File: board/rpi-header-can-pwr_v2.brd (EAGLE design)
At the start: 87 x 56.5 mm, 57 parts, among them U1 MCP2515, U2 ADS1015, U3 BME280, X1 RJ45-8L21-S, X2 RASPI_BOARD_B+#_E3

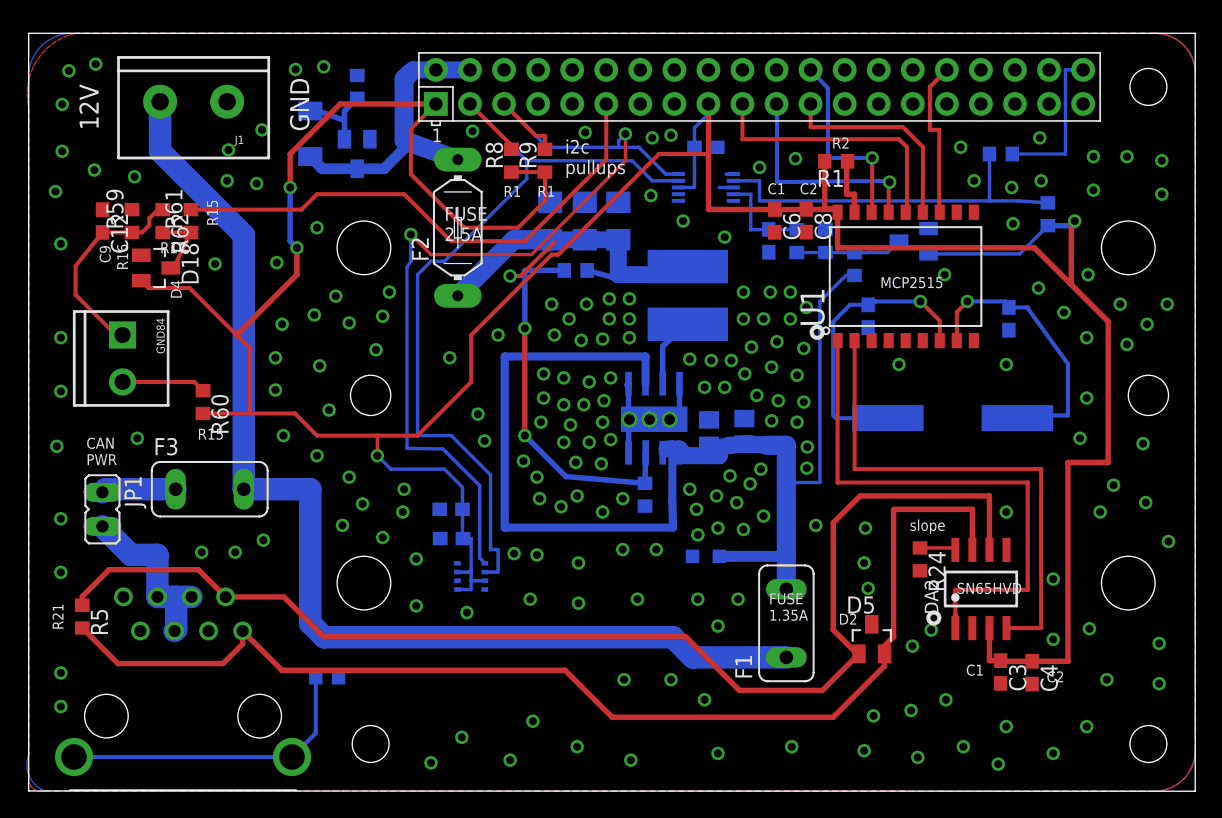
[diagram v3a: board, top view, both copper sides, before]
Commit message: change to microfit from rj45
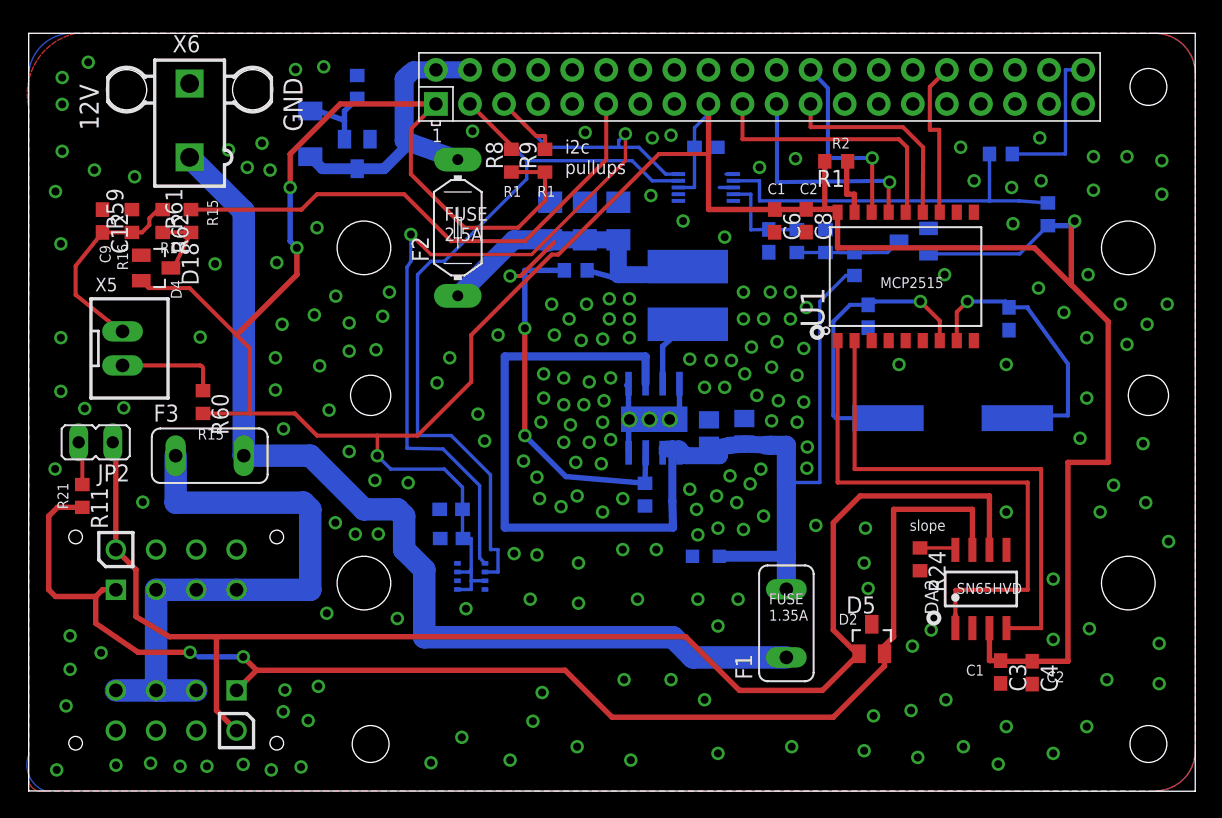
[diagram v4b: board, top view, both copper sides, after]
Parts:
- removed GND84: (no value), SparkFun-Connectors:SCREWTERMINAL-3.5MM-2
- removed J1: (no value), SparkFun-Connectors:SCREWTERMINAL-5MM-2
- removed JP1: (no value), jumper:JP1
- removed R25: 10k, rcl:R0603
- removed R5: 120, rcl:R0603
- removed X1: RJ45-8L21-S, con-tycoelectronics:RJ45-SHIELD1
- added JP2: (no value), jumper:JP1
- added R11: 120, rcl:R0603
- added X3, X4: (no value), con-molex-micro-fit-3_0:43045-0812
- added X5: JST-XH-02-PIN-LONG-PAD, Rembrandt Electronics - JST XH Connectors v1-0:JST-XH-02-PACKAGE-LONG-PAD
- added X6: 5566-2, con-molex:5566-2
- moved F3 2.50 mm to (13.5, 25.0)
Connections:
- removed net N$20: R25.1, X1.S1, X1.S2
- removed net N$5: F3.1, JP1.1
- removed net RJ45_12V: JP1.2, X1.4, X1.5, X1.6
- new net CAN_PWR: F3.1, X3.P$2, X3.P$3, X3.P$4, X4.P$2, X4.P$3, X4.P$4
- new net N$12: JP2.2, R11.1
- net CAN_H: now also R11.2, X3.P$1, X4.P$1; no longer R5.2, X1.1
- net CAN_L: now also JP2.1, X3.P$5, X4.P$5; no longer R5.1, X1.2
- net GND: now also X3.P$6, X3.P$7, X3.P$8, X4.P$6, X4.P$7, X4.P$8, X6.2; no longer J1.1, R25.2, X1.3, X1.7, X1.8
- net N$10: now also X5.2; no longer GND84.2
- net N$11: now also X5.1; no longer GND84.1
- net PRE_FUSE_12V: now also X6.1; no longer J1.2
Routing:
- net CAN_PWR: track 0.00 -> 45.0 mm
- net N$20: track 22.9 -> 0.00 mm
- net CAN_L: track 91.4 -> 105.6 mm
- net CAN_H: track 87.6 -> 101.7 mm, vias 0 -> 2
- net RJ45_12V: track 13.3 -> 0.00 mm
- net PRE_FUSE_12V: track 83.0 -> 75.0 mm
- net N$5: track 5.56 -> 0.00 mm
- net N$12: track 0.00 -> 3.26 mm
- net N$10: track 6.27 -> 7.75 mm
- net GND: vias 211 -> 225
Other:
- board text added: "CAN TERMINATION"
- board text removed: "CAN PWR"

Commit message: add lora support
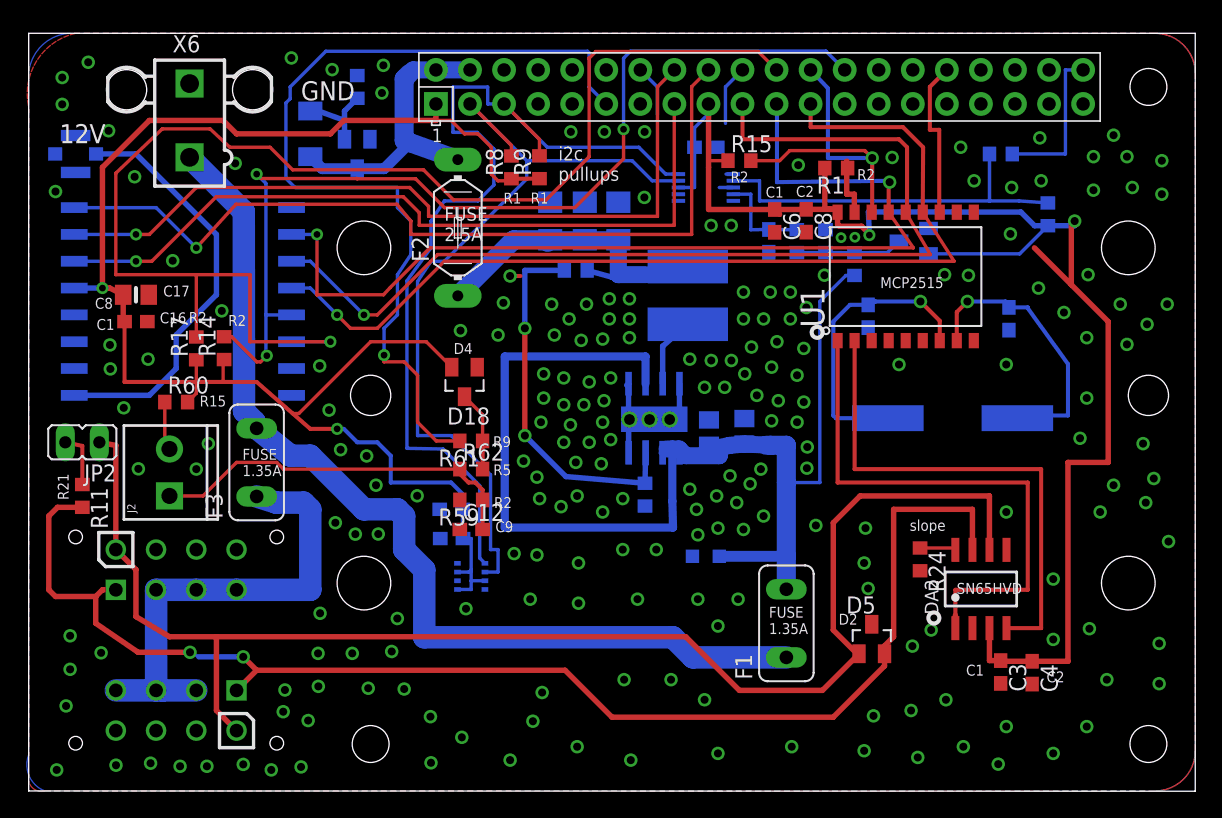
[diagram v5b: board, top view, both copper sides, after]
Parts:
- removed X5: JST-XH-02-PIN-LONG-PAD, Rembrandt Electronics - JST XH Connectors v1-0:JST-XH-02-PACKAGE-LONG-PAD
- added C16: 0.1uF, microbuilder:0603-NO
- added C17: 10uF, microbuilder:0805-NO
- added J1: U.FL, SparkFun-Connectors:U.FL
- added J2: (no value), SparkFun-Connectors:SCREWTERMINAL-3.5MM-2
- added R14, R15, R17: 10k, rcl:R0603
- added U4: RFM69HCW, microbuilder:RFMHCW_SMT
- moved C12 35.9 mm to (33.0, 19.5), turned to 0 degrees
- moved R59 32.8 mm to (33.0, 21.7), turned to 180 degrees
- moved R62 29.5 mm to (33.0, 24.0), turned to 0 degrees
- moved R61 26.6 mm to (33.0, 26.1), turned to 180 degrees
- moved D18 24.5 mm to (32.5, 30.5), turned to 180 degrees
- moved F3 3.54 mm to (17.0, 24.5), turned to 90 degrees
- moved R60 2.00 mm to (11.0, 29.0), turned to 0 degrees
- moved JP2 1.00 mm to (4.00, 26.0)
- moved R9 0.64 mm to (38.1, 46.5)
- moved R1 0.50 mm to (60.2, 46.5)
- moved R8 0.50 mm to (36.0, 46.5)
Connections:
- new net LORA_CS: R14.2, U4.13P, X2.26
- new net LORA_DIO0: U4.6P, X2.15
- new net LORA_DIO1: U4.7P, X2.16
- new net LORA_DIO2: U4.8P, X2.18
- new net LORA_RST: R17.2, U4.14P, X2.22
- new net N$5: J1.P$3, U4.1P
- net +3V3: now also C16.1, C17.1, R14.1, R15.1, R17.1, U4.5P
- net CAN_CS: now also R15.2
- net GND: now also C16.2, C17.2, J1.P$1, J1.P$2, U4.16P, U4.2P, U4.9P
- net MISO: now also U4.10P
- net MOSI: now also U4.11P
- net N$10: now also J2.2; no longer X5.2
- net N$11: now also J2.1; no longer X5.1
- net SCK: now also U4.12P
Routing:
- net LORA_RST: track 0.00 -> 98.3 mm, vias 0 -> 1
- net LORA_CS: track 0.00 -> 74.6 mm, vias 0 -> 3
- net LORA_DIO2: track 0.00 -> 63.1 mm, vias 0 -> 1
- net LORA_DIO1: track 0.00 -> 57.7 mm, vias 0 -> 1
- net LORA_DIO0: track 0.00 -> 57.2 mm, vias 0 -> 1
- net SCK: track 15.6 -> 72.7 mm, vias 0 -> 1
- net MISO: track 16.6 -> 72.2 mm, vias 1 -> 2
- net MOSI: track 20.1 -> 74.9 mm, vias 0 -> 1
- net N$5: track 0.00 -> 31.1 mm
- net TAMPER: track 39.6 -> 67.6 mm, vias 0 -> 1
- net N$11: track 15.3 -> 28.4 mm
- net +3V3: track 244.7 -> 231.7 mm
- net CAN_CS: track 14.5 -> 24.1 mm
- net CAN_PWR: track 45.0 -> 35.5 mm
- net GND: track 19.6 -> 24.4 mm, vias 225 -> 221
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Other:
- board text added: "8Mhz crystal"
- board text added: "C8"
- board text added: "CAN TERMI NATION"
- board text added: "R9"
- board text added: "RFM69HW"
- board text added: "can rpi header 2020.11.27 v1.5"
- board text added: "lora ant"
- board text removed: "CAN TERMINATION"
- board text removed: "R16"
- board text removed: "R17"
- board text removed: "can rpi header 2020.07.09 v1.4"
- board text removed: "shield"

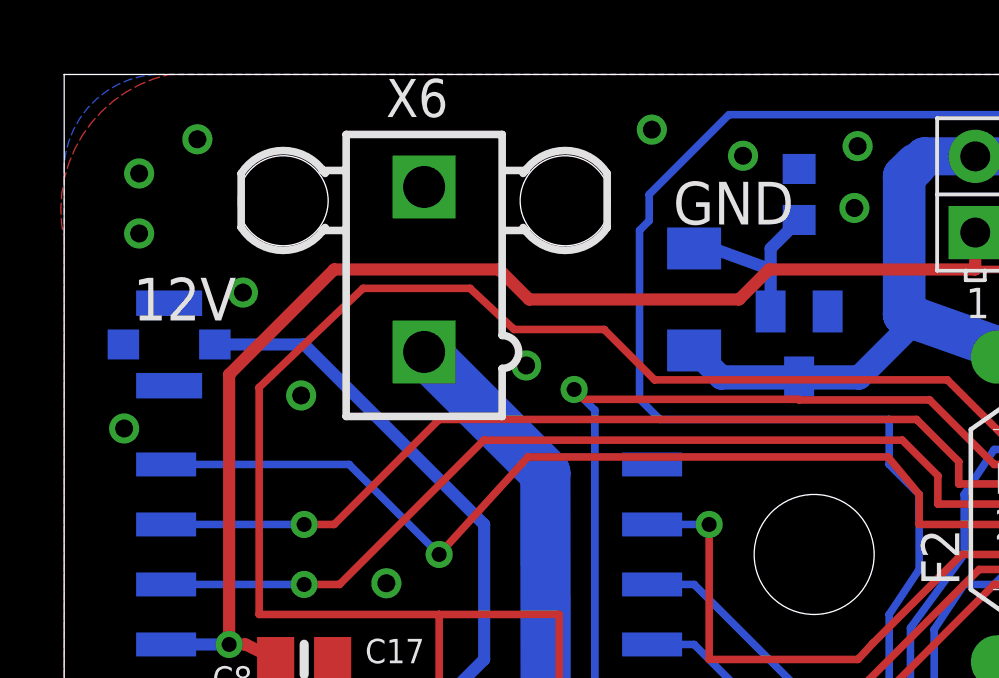
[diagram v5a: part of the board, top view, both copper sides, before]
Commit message: change power connector to 5mm screw terminal
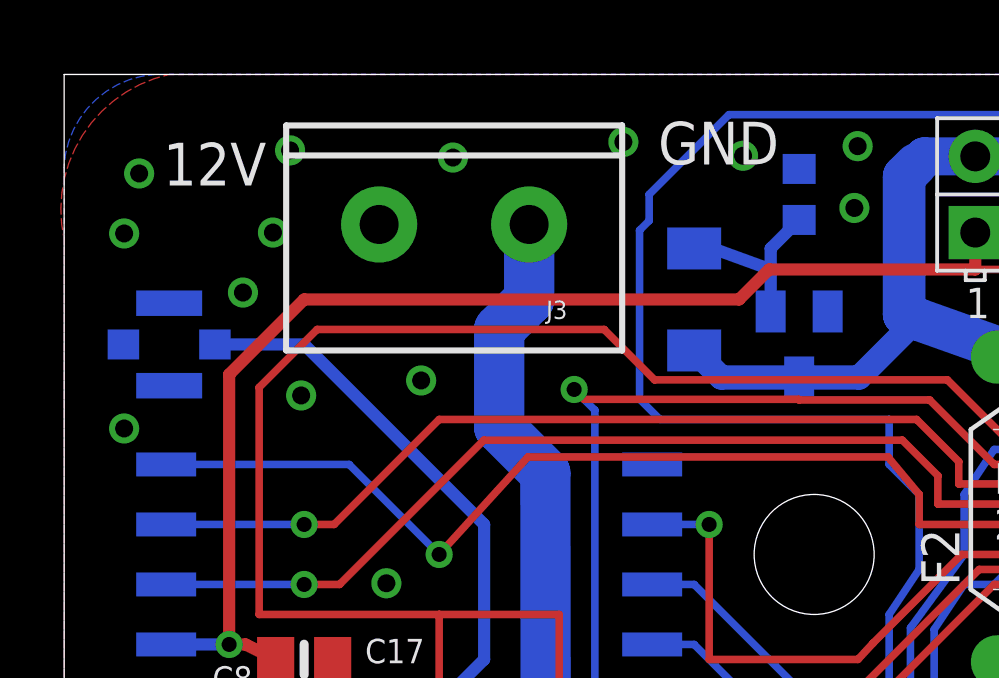
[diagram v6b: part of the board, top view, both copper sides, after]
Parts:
- removed X6: 5566-2, con-molex:5566-2
- added J3: (no value), SparkFun-Connectors:SCREWTERMINAL-5MM-2
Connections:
- net GND: now also J3.2; no longer X6.2
- net PRE_FUSE_12V: now also J3.1; no longer X6.1
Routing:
- net PRE_FUSE_12V: track 73.1 -> 76.7 mm
- net LORA_RST: track 98.3 -> 97.3 mm
- net +3V3: track 231.7 -> 230.9 mm
- net GND: vias 221 -> 223
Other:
- board text removed: "T3"
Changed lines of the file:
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@@
 <text x="31" y="41" size="1.016" layer="121">FUSE
 2.5A</text>
-<text x="2.3" y="48.3" size="1.4224" layer="121">12V</text>
-<text x="20.3" y="51.5" size="1.4224" layer="121">GND</text>
+<text x="3.3" y="52.8" size="1.4224" layer="121">12V</text>
+<text x="19.8" y="53.5" size="1.4224" layer="121">GND</text>
 <text x="33.1" y="33.4" size="0.8128" layer="121" rot="R180">D4</text>
 <text x="35.98" y="24.35" size="0.8128" layer="121" rot="R180">R5</text>
@@
 <text x="5.56" y="20.09" size="1.016" layer="122" rot="MR90">tamper</text>
 <text x="22.2" y="52.9" size="0.8128" layer="122" rot="MR180">R5</text>
-<text x="-20.7" y="46.4" size="0.8128" layer="122" rot="MR0">T3</text>
 <text x="20.2" y="52.6" size="0.8128" layer="122" rot="MR180">D6</text>
 <text x="15.94" y="23.48" size="0.8128" layer="121">FUSE
@@
 ALERT</text>
 <text x="26.2" y="46.6" size="0.8128" layer="122" rot="MR180">T2</text>
-<text x="6.3" y="48.3" size="1.4224" layer="122" rot="MR180">12V</text>
-<text x="19.2" y="47.5" size="1.4224" layer="122" rot="MR0">GND</text>
+<text x="3.3" y="54.3" size="1.4224" layer="122" rot="MR180">12V</text>
+<text x="23.7" y="53.5" size="1.4224" layer="122" rot="MR0">GND</text>
 <text x="76.4" y="40.3" size="0.8128" layer="122" rot="MR0">R1</text>
 <text x="55.97" y="38.36" size="0.8128" layer="122" rot="MR0">C9</text>
@@
 <circle x="1.86" y="28.2" radius="0.3" width="0.4064" layer="122"/>
 <text x="9.7" y="37.1" size="0.8128" layer="122" rot="MR0" align="bottom-right">RFM69HW</text>
-<text x="1.3" y="53.3" size="1.4224" layer="122" rot="MR180">lora
+<text x="5.7" y="49.7" size="1.4224" layer="122" distance="12" rot="MR0">lora
 ant</text>
 <text x="65.75" y="25.79" size="0.8128" layer="122" rot="MR180">8Mhz crystal</text>
@@
 <element name="R11" library="rcl" package="R0603" value="120" x="4" y="22" rot="R270"/>
 <element name="JP2" library="jumper" package="JP1" value="" x="4" y="26" rot="R90"/>
-<element name="X6" library="con-molex" package="5566-2" value="5566-2" x="12" y="50">
-<attribute name="MPN" value="" x="12" y="50" size="1.778" layer="27" display="off"/>
-<attribute name="OC_NEWARK" value="unknown" x="12" y="50" size="1.778" layer="27" display="off"/>
-<attribute name="MF" value="" x="12" y="50" size="1.778" layer="27" display="off"/>
-<attribute name="OC_FARNELL" value="1822072" x="12" y="50" size="1.778" layer="27" display="off"/>
-</element>
 <element name="U4" library="microbuilder" package="RFMHCW_SMT" value="RFM69HCW" x="11.5" y="36.5" rot="MR0"/>
 <element name="C17" library="microbuilder" package="0805-NO" value="10uF" x="8" y="37"/>
@@
 <element name="J2" library="SparkFun-Connectors" package="SCREWTERMINAL-3.5MM-2" value="" x="10.5" y="22" rot="R90">
 <attribute name="PROD_ID" value="CONN-08399" x="10.5" y="22" size="1.778" layer="27" rot="R90" display="off"/>
+</element>
+<element name="J3" library="SparkFun-Connectors" package="SCREWTERMINAL-5MM-2" value="" x="15.5" y="51.5" rot="R180">
+<attribute name="SF_SKU" value="PRT-08432" x="15.5" y="51.5" size="1.778" layer="27" rot="R180" display="off"/>
 </element>
 </elements>
@@
 <contactref element="C17" pad="1"/>
 <contactref element="C16" pad="1"/>
-<wire x1="14.5" y1="50" x2="9" y2="50" width="0.4064" layer="1"/>
 <wire x1="5.5" y1="46.5" x2="5.5" y2="37.5" width="0.4064" layer="1"/>
 <wire x1="3.4" y1="37.5" x2="5.5" y2="37.5" width="0.4064" layer="16"/>
@@
 <wire x1="52.15" y1="47" x2="50.7" y2="47" width="0.254" layer="1"/>
 <wire x1="50.7" y1="47" x2="50.7" y2="46.5" width="0.254" layer="1"/>
-<wire x1="9" y1="50" x2="5.5" y2="46.5" width="0.4064" layer="1"/>
+<wire x1="8" y1="49" x2="5.5" y2="46.5" width="0.4064" layer="1"/>
 <wire x1="60.32" y1="42.25" x2="60.46" y2="42.11" width="0.4064" layer="1"/>
 <wire x1="60.46" y1="42.11" x2="62.11" y2="42.11" width="0.4064" layer="1"/>
@@
 <wire x1="14.5" y1="32.1" x2="14.5" y2="30.5" width="0.254" layer="1"/>
 <wire x1="12.5" y1="32.15" x2="12.5" y2="30.5" width="0.254" layer="1"/>
-<wire x1="14.5" y1="50" x2="15.5" y2="49" width="0.4064" layer="1"/>
-<wire x1="15.5" y1="49" x2="22.5" y2="49" width="0.4064" layer="1"/>
 <wire x1="22.5" y1="49" x2="23.5" y2="50" width="0.4064" layer="1"/>
 <wire x1="30.37" y1="50" x2="31.5" y2="50" width="0.254" layer="1"/>
@@
 <wire x1="62.5" y1="41.5" x2="62.55" y2="41.45" width="0.254" layer="1"/>
 <wire x1="62.55" y1="41.45" x2="62.69" y2="41.45" width="0.254" layer="1"/>
+<wire x1="22.5" y1="49" x2="8" y2="49" width="0.4064" layer="1"/>
 <wire x1="38.09" y1="45.66" x2="48.45" y2="45" width="0" layer="19" extent="1-16"/>
 </signal>
@@
 <via x="42.8" y="33.7" extent="1-16" drill="0.6"/>
 <via x="8.9" y="32.2" extent="1-16" drill="0.6"/>
-<via x="19.59" y="54.66" extent="1-16" drill="0.6"/>
-<via x="4.44" y="54.34" extent="1-16" drill="0.6"/>
+<via x="18.64" y="54.25" extent="1-16" drill="0.6"/>
+<via x="7.53" y="53.97" extent="1-16" drill="0.6"/>
 <via x="46.3" y="27.7" extent="1-16" drill="0.8"/>
 <via x="44.8" y="27.7" extent="1-16" drill="0.8"/>
@@
 <contactref element="X2" pad="34"/>
 <contactref element="X2" pad="39"/>
-<via x="2.5" y="51.2" extent="1-16" drill="0.6"/>
+<via x="2" y="51.2" extent="1-16" drill="0.6"/>
 <via x="6.06" y="33.26" extent="1-16" drill="0.6"/>
 <via x="25.2" y="24.98" extent="1-16" drill="0.6"/>
 <via x="7.9" y="45.8" extent="1-16" drill="0.6"/>
-<via x="15.4" y="46.8" extent="1-16" drill="0.6"/>
+<via x="11.9" y="46.3" extent="1-16" drill="0.6"/>
 <via x="5.96" y="49.23" extent="1-16" drill="0.6"/>
 <via x="10.74" y="39.54" extent="1-16" drill="0.6"/>
@@
 <via x="38.29" y="7.34" extent="1-16" drill="0.6"/>
 <via x="16" y="1.98" extent="1-16" drill="0.6"/>
-<contactref element="X6" pad="2"/>
 <contactref element="U4" pad="16P"/>
 <contactref element="U4" pad="2P"/>
@@
 <wire x1="45.61" y1="53.77" x2="46.89" y2="52.49" width="0.254" layer="16"/>
 <wire x1="46.89" y1="52.49" x2="46.89" y2="50.43" width="0.254" layer="16"/>
+<contactref element="J3" pad="2"/>
+<via x="6.96" y="51.23" extent="1-16" drill="0.6"/>
+<via x="12.96" y="53.73" extent="1-16" drill="0.6"/>
 </signal>
 <signal name="CAN_TX">
@@
 <wire x1="29.5" y1="16.5" x2="29.5" y2="11.46" width="1.6764" layer="16"/>
 <contactref element="F1" pad="1"/>
-<contactref element="X6" pad="1"/>
-<wire x1="16.04" y1="43.21" x2="12" y2="47.25" width="1.6764" layer="16"/>
 <wire x1="56.5" y1="9.96" x2="49.54" y2="9.96" width="1.6764" layer="16"/>
 <wire x1="21" y1="25" x2="19.54" y2="25" width="1.6764" layer="16"/>
@@
 <wire x1="17" y1="27.04" x2="16.84" y2="27.54" width="1.6764" layer="16"/>
 <wire x1="16.84" y1="27.54" x2="16.06" y2="28.32" width="1.6764" layer="16"/>
+<contactref element="J3" pad="1"/>
+<wire x1="16.04" y1="43.21" x2="14.5" y2="44.75" width="1.6764" layer="16"/>
+<wire x1="14.5" y1="44.75" x2="14.5" y2="48" width="1.6764" layer="16"/>
+<wire x1="14.5" y1="48" x2="15.5" y2="49" width="1.6764" layer="16"/>
+<wire x1="15.5" y1="49" x2="15.5" y2="51.5" width="1.6764" layer="16"/>
 </signal>
 <signal name="I2C_SDA">
@@
 <wire x1="12.5" y1="38.5" x2="16.5" y2="38.5" width="0.254" layer="1"/>
 <wire x1="16.5" y1="38.5" x2="16.5" y2="33.5" width="0.254" layer="1"/>
-<wire x1="9.961925" y1="49.37" x2="6.5" y2="46.068075" width="0.254" layer="1"/>
 <wire x1="19.68" y1="46.32" x2="18" y2="48" width="0.254" layer="1"/>
-<wire x1="18" y1="48" x2="15" y2="48" width="0.254" layer="1"/>
-<wire x1="15" y1="48" x2="13.53" y2="49.37" width="0.254" layer="1"/>
-<wire x1="13.53" y1="49.37" x2="9.961925" y2="49.37" width="0.254" layer="1"/>
 <wire x1="12.5" y1="33.85" x2="12.5" y2="38.5" width="0.254" layer="1"/>
+<wire x1="18" y1="48" x2="8.431925" y2="48" width="0.254" layer="1"/>
+<wire x1="8.431925" y1="48" x2="6.5" y2="46.068075" width="0.254" layer="1"/>
 </signal>
 </signals>
